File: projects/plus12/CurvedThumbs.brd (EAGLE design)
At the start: 123.8 x 54 mm, 14 parts

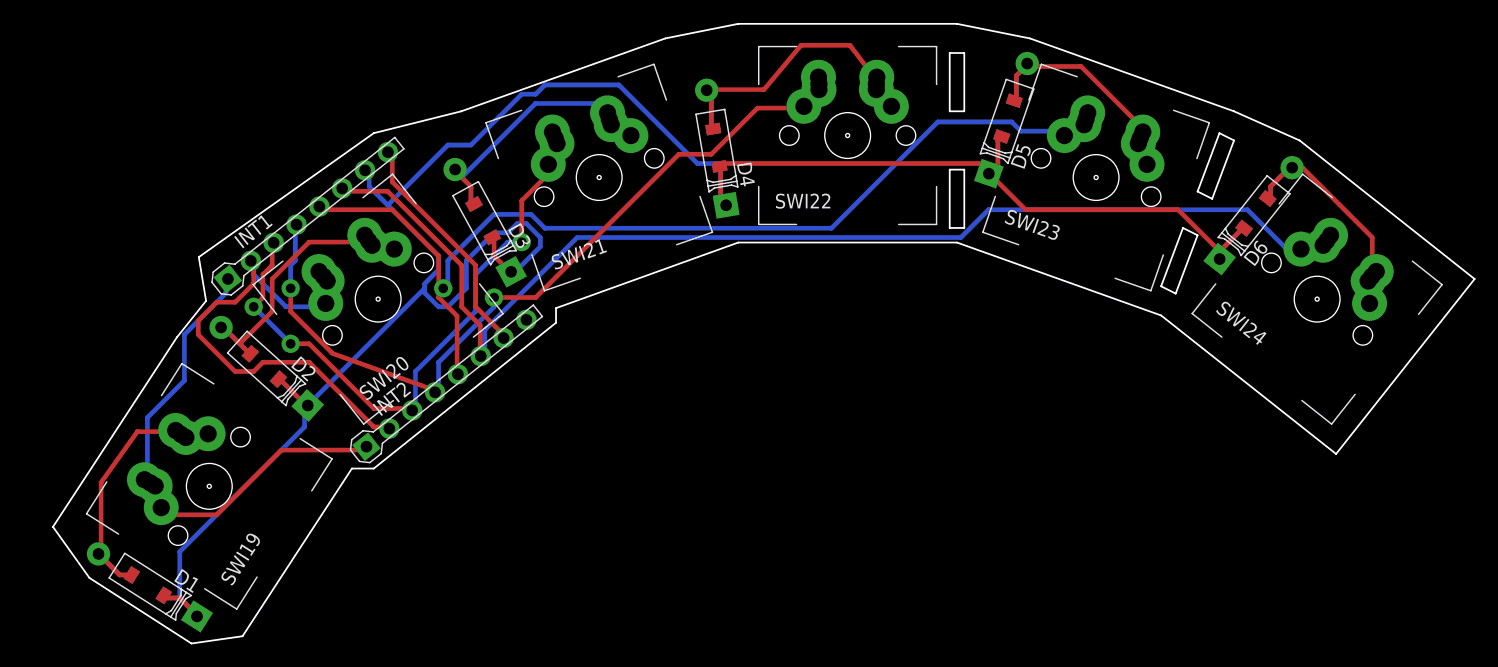
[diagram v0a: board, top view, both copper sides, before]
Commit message: Adding 3 thumb option
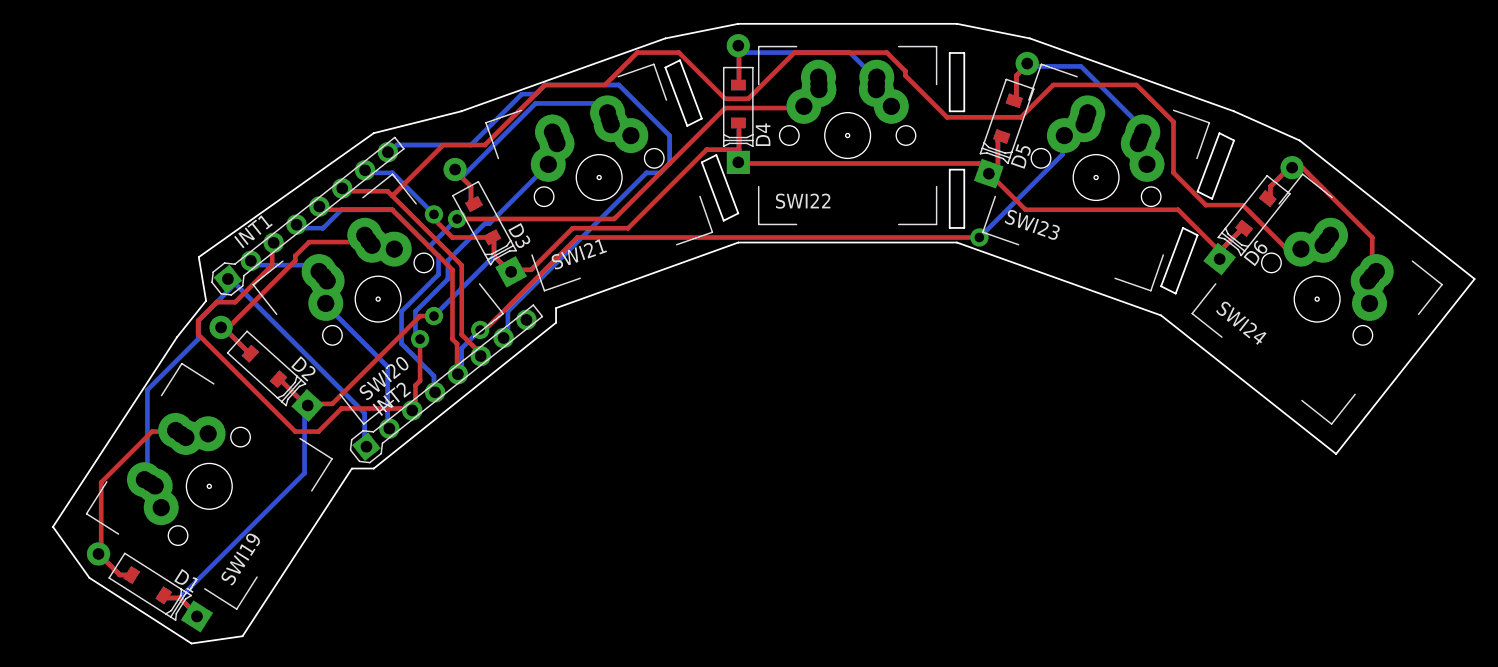
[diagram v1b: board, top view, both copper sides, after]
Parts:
- moved D4 4.26 mm to (60.3, 48.3), turned to 90 degrees
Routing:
- net N$14: track 20.4 -> 53.1 mm
- net N$13: track 194.7 -> 171.4 mm, vias 0 -> 2
- net N$12: track 105.3 -> 125.9 mm
- net N$8: track 43.4 -> 25.5 mm
- net N$9: track 54.7 -> 65.7 mm, vias 3 -> 1
- net N$4: track 25.2 -> 20.5 mm
- net N$7: track 46.7 -> 45.2 mm
- net N$11: track 90.1 -> 90.4 mm, vias 1 -> 2
- net N$10: track 70.9 -> 71.0 mm, vias 2 -> 1
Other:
- outline, holes or cut-outs redrawn

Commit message: switching headers
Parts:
- removed INT2: INTRCNNT, Keys:INTRCNNT
- INT1: value INTRCNNT -> INTRCNNT4X2; device Keys:INTRCNNT -> Keys:INTRRIBBON
- moved INT1 12.6 mm to (24.8, 41.9), turned to 218.4 degrees
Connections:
- removed net N$14: INT1.T2, INT2.T1
- net N$10: no longer INT2.C4
- net N$11: no longer INT2.C5
- net N$12: no longer INT2.C6
- net N$7: no longer INT2.C1
- net N$8: no longer INT2.C2
- net N$9: no longer INT2.C3
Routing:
- net N$13: track 171.4 -> 0.00 mm, vias 2 -> 0
- net N$12: track 125.9 -> 0.00 mm
- net N$11: track 90.4 -> 0.00 mm, vias 2 -> 0
- net N$10: track 71.0 -> 0.00 mm, vias 1 -> 0
- net N$9: track 65.7 -> 0.00 mm, vias 1 -> 0
- net N$14: track 53.1 -> 0.00 mm
- net N$7: track 45.2 -> 0.00 mm
- net N$8: track 25.5 -> 0.00 mm
- net N$2: track 24.0 -> 0.00 mm
- net N$3: track 23.9 -> 0.00 mm
- net N$1: track 22.0 -> 0.00 mm
- net N$5: track 21.4 -> 0.00 mm
- net N$6: track 20.7 -> 0.00 mm
- net N$4: track 20.5 -> 0.00 mm
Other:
- board size 123.8 x 54 mm -> 126.4 x 54 mm
- board text added: "Plus12 Aleutian Keylands"

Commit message: switching interconnects
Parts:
- moved INT1 8.03 mm to (17.1, 39.4), turned to 38.4 degrees
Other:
- board size 126.4 x 54 mm -> 123.2 x 54 mm
- board text added: "Aleutian Key- lands"
- board text added: "Plus12"
- board text removed: "Plus12 Aleutian Keylands"
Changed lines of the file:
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@@
 <wire x1="60.325" y1="55.245" x2="53.975" y2="53.975" width="0.1524" layer="20"/>
 <wire x1="53.975" y1="53.975" x2="35.56" y2="48.26" width="0.1524" layer="20"/>
-<wire x1="8.89" y1="31.115" x2="-1.905" y2="14.605" width="0.1524" layer="20"/>
-<wire x1="-1.905" y1="14.605" x2="3.81" y2="6.985" width="0.1524" layer="20"/>
+<wire x1="11.43" y1="28.575" x2="1.27" y2="12.065" width="0.1524" layer="20"/>
+<wire x1="1.27" y1="12.065" x2="3.81" y2="6.985" width="0.1524" layer="20"/>
 <wire x1="3.81" y1="6.985" x2="12.7" y2="1.27" width="0.1524" layer="20"/>
 <wire x1="12.7" y1="1.27" x2="17.145" y2="1.905" width="0.1524" layer="20"/>
@@
 <wire x1="79.375" y1="36.195" x2="97.155" y2="29.845" width="0.1524" layer="20"/>
 <wire x1="97.155" y1="29.845" x2="112.395" y2="17.78" width="0.1524" layer="20"/>
-<wire x1="8.89" y1="31.115" x2="12.7" y2="36.83" width="0.1524" layer="20"/>
-<wire x1="12.7" y1="36.83" x2="14.605" y2="40.005" width="0.1524" layer="20"/>
+<wire x1="11.43" y1="28.575" x2="15.24" y2="33.02" width="0.1524" layer="20"/>
+<wire x1="15.24" y1="33.02" x2="14.605" y2="40.005" width="0.1524" layer="20"/>
 <wire x1="14.605" y1="40.005" x2="22.86" y2="46.355" width="0.1524" layer="20"/>
 <wire x1="22.86" y1="46.355" x2="30.48" y2="45.085" width="0.1524" layer="20"/>
@@
 <wire x1="103.505" y1="47.625" x2="97.155" y2="29.845" width="0.1524" layer="21"/>
 <wire x1="97.155" y1="29.845" x2="103.505" y2="47.625" width="0.1524" layer="22"/>
-<text x="12.7" y="28.575" size="1.778" layer="22" rot="MR302.4">Plus12
-Aleutian Keylands</text>
-<text x="2.54" y="12.065" size="1.778" layer="21" rot="R57.6">Plus12
-Aleutian Keylands</text>
+<text x="19.05" y="15.875" size="1.778" layer="22" rot="MR302.4">Plus12</text>
+<text x="15.24" y="9.525" size="1.778" layer="21" rot="R57.6">Plus12</text>
+<text x="34.29" y="23.495" size="1.778" layer="21" rot="R38.4">Aleutian
+Key-
+lands</text>
+<text x="34.925" y="24.13" size="1.778" layer="22" rot="MR321.6">Aleutian
+Key-
+lands</text>
 </plain>
 <attributes>
@@
 <element name="D5" library="Keys" library_urn="urn:adsk.eagle:library:1331239" package="DIODE_COMBO" package3d_urn="urn:adsk.eagle:package:3624144/3" value="DIODE" x="83.82" y="46.99" rot="R70.8"/>
 <element name="D6" library="Keys" library_urn="urn:adsk.eagle:library:1331239" package="DIODE_COMBO" package3d_urn="urn:adsk.eagle:package:3624144/3" value="DIODE" x="105.41" y="38.735" rot="R51.6"/>
-<element name="INT1" library="Keys" library_urn="urn:adsk.eagle:library:1331239" package="INTRRIBBON" value="INTRCNNT4X2" x="24.765" y="41.91" rot="R218.4"/>
+<element name="INT1" library="Keys" library_urn="urn:adsk.eagle:library:1331239" package="INTRRIBBON" value="INTRCNNT4X2" x="17.145" y="39.37" rot="R38.4"/>
 <element name="SWI19" library="Keys" library_urn="urn:adsk.eagle:library:1331239" package="DOUBLED_MX/ALPS" package3d_urn="urn:adsk.eagle:package:1435773/5" value="MX/ALPSDOUBLESIDED" x="14.2494" y="14.9606" rot="R57.6"/>
 <element name="SWI20" library="Keys" library_urn="urn:adsk.eagle:library:1331239" package="DOUBLED_MX/ALPS" package3d_urn="urn:adsk.eagle:package:1435773/5" value="MX/ALPSDOUBLESIDED" x="28.956" y="31.2674" rot="R38.4"/>
@@
 <contactref element="SWI19" pad="LCL"/>
 <contactref element="SWI19" pad="LCR"/>
-<wire x1="8.5992125" y1="15.53800625" x2="24.765" y2="41.91" width="0" layer="19" extent="1-1"/>
+<wire x1="8.5992125" y1="15.53800625" x2="17.145" y2="39.37" width="0" layer="19" extent="1-1"/>
 <wire x1="9.11035625" y1="15.261" x2="8.5992125" y2="15.53800625" width="0" layer="19" extent="1-1"/>
 <wire x1="9.53251875" y1="14.993084375" x2="9.11035625" y2="15.261" width="0" layer="19" extent="1-1"/>
@@
 <wire x1="23.8099875" y1="33.670846875" x2="24.2016" y2="33.24115" width="0" layer="19" extent="1-1"/>
 <wire x1="24.3924125" y1="30.89140625" x2="24.512175" y2="32.849303125" width="0" layer="19" extent="1-1"/>
-<wire x1="22.774415625" y1="40.332284375" x2="23.8099875" y2="33.670846875" width="0" layer="19" extent="1-1"/>
+<wire x1="19.13558125" y1="40.9477125" x2="23.8099875" y2="33.670846875" width="0" layer="19" extent="1-1"/>
 </signal>
 <signal name="N$9">
@@
 <wire x1="44.532790625" y1="44.8145375" x2="44.36835625" y2="45.286725" width="0" layer="19" extent="1-1"/>
 <wire x1="43.775803125" y1="43.00493125" x2="44.532790625" y2="44.8145375" width="0" layer="19" extent="1-1"/>
-<wire x1="20.783834375" y1="38.75456875" x2="43.775803125" y2="43.00493125" width="0" layer="19" extent="1-1"/>
+<wire x1="21.1261625" y1="42.525428125" x2="43.775803125" y2="43.00493125" width="0" layer="19" extent="1-1"/>
 </signal>
 <signal name="N$10">
@@
 <wire x1="67.31" y1="50.5968" x2="67.35" y2="50.0168" width="0" layer="19" extent="1-1"/>
 <wire x1="66.04" y1="48.0568" x2="67.35" y2="49.5168" width="0" layer="19" extent="1-1"/>
-<wire x1="18.793253125" y1="37.176853125" x2="66.04" y2="48.0568" width="0" layer="19" extent="1-1"/>
+<wire x1="23.11674375" y1="44.10314375" x2="66.04" y2="48.0568" width="0" layer="19" extent="1-1"/>
 </signal>
 <signal name="N$11">
@@
 <wire x1="90.762725" y1="47.491953125" x2="90.60975625" y2="46.931059375" width="0" layer="19" extent="1-1"/>
 <wire x1="88.728046875" y1="45.510896875" x2="90.445325" y2="46.458871875" width="0" layer="19" extent="1-1"/>
-<wire x1="23.187284375" y1="43.90058125" x2="88.728046875" y2="45.510896875" width="0" layer="19" extent="1-1"/>
+<wire x1="18.7227125" y1="37.379415625" x2="88.728046875" y2="45.510896875" width="0" layer="19" extent="1-1"/>
 </signal>
 <signal name="N$12">
@@
 <wire x1="111.26935625" y1="35.955040625" x2="111.57993125" y2="36.3468875" width="0" layer="19" extent="1-1"/>
 <wire x1="109.335840625" y1="35.624553125" x2="111.26935625" y2="35.955040625" width="0" layer="19" extent="1-1"/>
-<wire x1="21.196703125" y1="42.322865625" x2="109.335840625" y2="35.624553125" width="0" layer="19" extent="1-1"/>
+<wire x1="20.71329375" y1="38.95713125" x2="109.335840625" y2="35.624553125" width="0" layer="19" extent="1-1"/>
 </signal>
 <signal name="N$13">
@@
 <wire x1="38.892846875" y1="36.65183125" x2="40.539534375" y2="33.644096875" width="0" layer="19" extent="16-16"/>
 <wire x1="38.892846875" y1="36.65183125" x2="38.892846875" y2="36.65183125" width="0" layer="19" extent="1-16"/>
-<wire x1="19.20611875" y1="40.74515" x2="38.892846875" y2="36.65183125" width="0" layer="19" extent="16-16"/>
-<wire x1="20.27693125" y1="24.2952625" x2="19.20611875" y2="40.74515" width="0" layer="19" extent="16-16"/>
+<wire x1="22.703878125" y1="40.534846875" x2="38.892846875" y2="36.65183125" width="0" layer="19" extent="16-16"/>
+<wire x1="20.27693125" y1="24.2952625" x2="22.703878125" y2="40.534846875" width="0" layer="19" extent="16-16"/>
 <wire x1="20.27693125" y1="24.2952625" x2="20.27693125" y2="24.2952625" width="0" layer="19" extent="1-16"/>
 <wire x1="22.825175" y1="22.000815625" x2="20.27693125" y2="24.2952625" width="0" layer="19" extent="16-16"/>

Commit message: Getting ready for pictures
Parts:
- added U$1: (no value), Logos:3_8INCH_TOP
- added U$2: (no value), Logos:3_8INCH_BOT
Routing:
- net N$13: track 0.00 -> 188.8 mm, vias 0 -> 3
- net N$12: track 0.00 -> 93.6 mm
- net N$11: track 0.00 -> 79.3 mm
- net N$10: track 0.00 -> 50.0 mm
- net N$7: track 0.00 -> 31.8 mm
- net N$9: track 0.00 -> 28.7 mm
- net N$2: track 0.00 -> 23.2 mm
- net N$3: track 0.00 -> 22.4 mm
- net N$1: track 0.00 -> 21.5 mm
- net N$5: track 0.00 -> 21.1 mm
- net N$4: track 0.00 -> 20.6 mm
- net N$6: track 0.00 -> 20.3 mm
- net N$8: track 0.00 -> 14.5 mm

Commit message: more updates than should be in one commit, lots of work
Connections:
- net N$1: now also SWI19.RLMID
- net N$10: now also SWI22.LLP, SWI22.LRLP
- net N$11: now also SWI23.LLP, SWI23.LRLP
- net N$12: now also SWI24.LLP, SWI24.LRLP
- net N$2: now also SWI20.RLMID
- net N$3: now also SWI21.RLMID
- net N$4: now also SWI22.RLMID
- net N$5: now also SWI23.RLMID
- net N$6: now also SWI24.RLMID
- net N$7: now also SWI19.LLP, SWI19.LRLP
- net N$8: now also SWI20.LLP, SWI20.LRLP
- net N$9: now also SWI21.LLP, SWI21.LRLP
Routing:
- net N$12: track 93.6 -> 113.4 mm
- net N$9: track 28.7 -> 45.6 mm
- net N$10: track 50.0 -> 66.0 mm
- net N$8: track 14.5 -> 29.9 mm
- net N$11: track 79.3 -> 94.3 mm
- net N$6: track 20.3 -> 34.6 mm
- net N$1: track 21.5 -> 35.8 mm
- net N$4: track 20.6 -> 34.3 mm
- net N$7: track 31.8 -> 44.9 mm
- net N$5: track 21.1 -> 34.1 mm
- net N$3: track 22.4 -> 34.7 mm
- net N$2: track 23.2 -> 35.0 mm
- net N$13: track 188.8 -> 194.3 mm, vias 3 -> 0
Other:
- outline, holes or cut-outs redrawn
- board text added: "Aleutian Keylands"
- board text removed: "Aleutian Key- lands"

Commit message: more updates than should be in one commit, lots of work
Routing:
- net N$13: track 194.3 -> 191.6 mm
- net N$2: track 35.0 -> 36.4 mm
- net N$12: track 113.4 -> 112.9 mm
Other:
- board size 123.2 x 54 mm -> 122.3 x 53.9 mm
